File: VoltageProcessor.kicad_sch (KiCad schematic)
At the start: 29 parts, among them J1 PJ301M-12, J2 PJ301M-12, J3 Eurorack power, J4 PJ301M-12, J5 PJ301M-12, U1 TL074

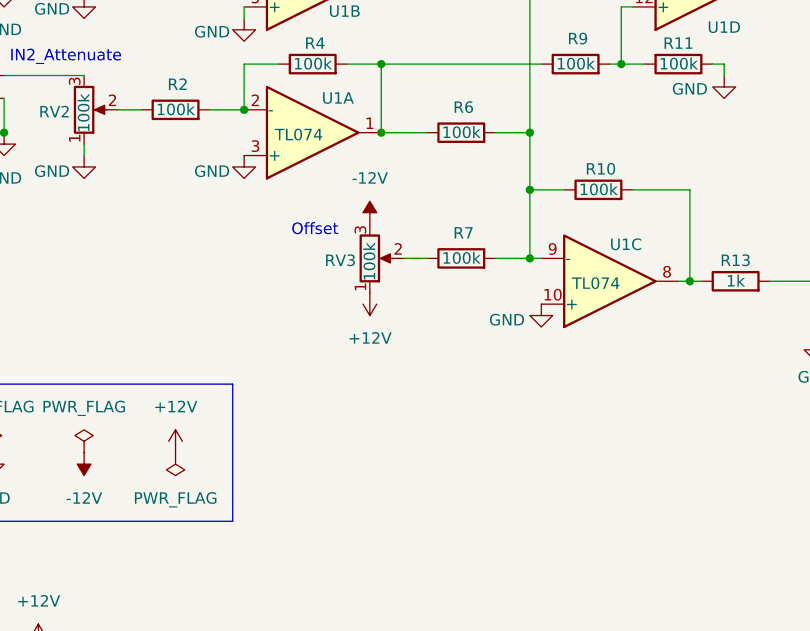
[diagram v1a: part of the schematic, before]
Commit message: Add `R15` `R16` to DC Offset potmeter its range is now `+-10` instead of the `rail-rail` voltage. Add small changes in routing to accomodate the resistors. Add change text to `rev 0.3`
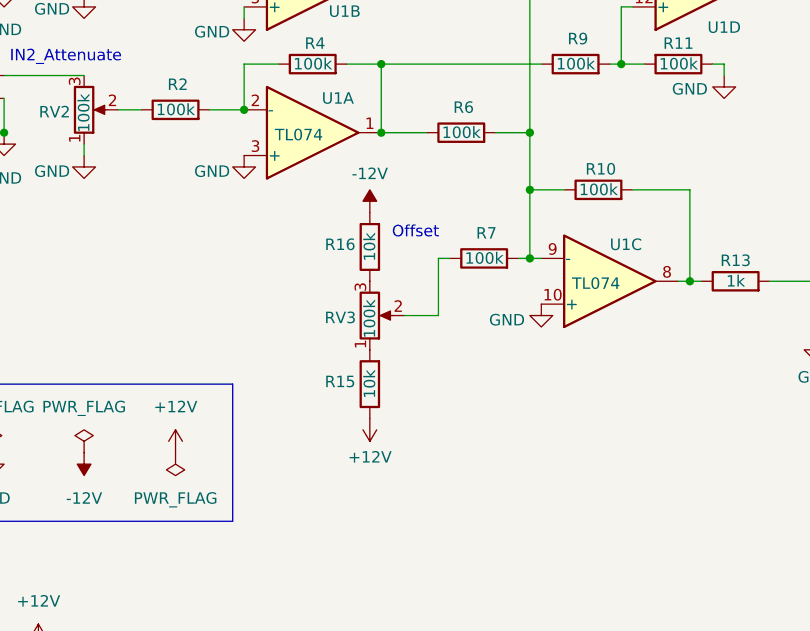
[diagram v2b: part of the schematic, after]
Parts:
- added R15, R16: 10k, Resistor_THT:R_Axial_DIN0204_L3.6mm_D1.6mm_P7.62mm_Horizontal, symbol Device:R
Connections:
- net +12V: now also R15.1; no longer RV3.1
- net -12V: now also R16.2; no longer RV3.3
- new net: R15.2, RV3.1
- new net: R16.1, RV3.3
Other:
- moved on the sheet: R7, RV3
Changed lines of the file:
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@@
 	)
 	(junction
-		(at 26.67 128.27)
+		(at 128.27 68.58)
 		(diameter 0)
 		(color 0 0 0 0)
 	)
 	(junction
-		(at 128.27 68.58)
+		(at 26.67 128.27)
 		(diameter 0)
 		(color 0 0 0 0)
@@
 	(wire
 		(pts
+			(xy 118.11 68.58) (xy 119.38 68.58)
+		)
+		(stroke
+			(width 0)
+			(type default)
+		)
+	)
+	(wire
+		(pts
 			(xy 82.55 35.56) (xy 85.09 35.56)
 		)
@@
 	(wire
 		(pts
+			(xy 114.3 74.93) (xy 118.11 74.93)
+		)
+		(stroke
+			(width 0)
+			(type default)
+		)
+	)
+	(wire
+		(pts
 			(xy 107.95 30.48) (xy 111.76 30.48)
 		)
@@
 	(wire
 		(pts
+			(xy 118.11 68.58) (xy 118.11 74.93)
+		)
+		(stroke
+			(width 0)
+			(type default)
+		)
+	)
+	(wire
+		(pts
 			(xy 129.54 68.58) (xy 128.27 68.58)
 		)
@@
 		)
 	)
-	(wire
-		(pts
-			(xy 114.3 68.58) (xy 116.84 68.58)
-		)
-		(stroke
-			(width 0)
-			(type default)
-		)
-	)
 	(polyline
 		(pts
@@
 	(wire
 		(pts
-			(xy 156.21 38.1) (xy 157.48 38.1)
+			(xy 127 68.58) (xy 128.27 68.58)
 		)
 		(stroke
@@
 	(wire
 		(pts
-			(xy 92.71 52.07) (xy 96.52 52.07)
+			(xy 156.21 38.1) (xy 157.48 38.1)
 		)
 		(stroke
@@
 	(wire
 		(pts
-			(xy 124.46 68.58) (xy 128.27 68.58)
+			(xy 92.71 52.07) (xy 96.52 52.07)
 		)
 		(stroke
@@
 	(text "Offset"
 		(exclude_from_sim no)
-		(at 104.394 65.532 0)
+		(at 115.57 65.786 0)
 		(effects
 			(font
@@
 	(symbol
 		(lib_id "power:+12V")
-		(at 110.49 72.39 180)
+		(at 110.49 86.36 180)
 		(unit 1)
 		(exclude_from_sim no)
@@
 		(on_board yes)
 		(dnp no)
-		(fields_autoplaced yes)
 		(property "Reference" "#PWR016"
-			(at 110.49 68.58 0)
+			(at 110.49 82.55 0)
 			(effects
 				(font
@@
 		)
 		(property "Value" "+12V"
-			(at 110.49 77.47 0)
+			(at 110.49 90.678 0)
 			(effects
 				(font
@@
 		)
 		(property "Footprint" ""
-			(at 110.49 72.39 0)
+			(at 110.49 86.36 0)
 			(effects
 				(font
@@
 		)
 		(property "Datasheet" ""
-			(at 110.49 72.39 0)
+			(at 110.49 86.36 0)
 			(effects
 				(font
@@
 		)
 		(property "Description" "Power symbol creates a global label with name \"+12V\""
-			(at 110.49 72.39 0)
+			(at 110.49 86.36 0)
 			(effects
 				(font
@@
 	(symbol
 		(lib_id "Device:R")
-		(at 120.65 68.58 90)
+		(at 123.19 68.58 90)
 		(unit 1)
 		(exclude_from_sim no)
@@
 		(dnp no)
 		(property "Reference" "R7"
-			(at 120.904 65.786 90)
+			(at 123.444 65.786 90)
 			(effects
 				(font
@@
 		)
 		(property "Value" "100k"
-			(at 120.65 68.58 90)
+			(at 123.19 68.58 90)
 			(effects
 				(font
@@
 		)
 		(property "Footprint" "Resistor_THT:R_Axial_DIN0204_L3.6mm_D1.6mm_P7.62mm_Horizontal"
-			(at 120.65 70.358 90)
+			(at 123.19 70.358 90)
 			(effects
 				(font
@@
 		)
 		(property "Datasheet" "~"
-			(at 120.65 68.58 0)
+			(at 123.19 68.58 0)
 			(effects
 				(font
@@
 		)
 		(property "Description" "Resistor"
-			(at 120.65 68.58 0)
+			(at 123.19 68.58 0)
 			(effects
 				(font
@@
 	(symbol
 		(lib_id "power:-12V")
-		(at 110.49 64.77 0)
+		(at 110.49 63.5 0)
 		(unit 1)
 		(exclude_from_sim no)
@@
 		(on_board yes)
 		(dnp no)
-		(fields_autoplaced yes)
 		(property "Reference" "#PWR015"
-			(at 110.49 68.58 0)
+			(at 110.49 67.31 0)
 			(effects
 				(font
@@
 		)
 		(property "Value" "-12V"
-			(at 110.49 59.69 0)
+			(at 110.49 59.182 0)
 			(effects
 				(font
@@
 		)
 		(property "Footprint" ""
-			(at 110.49 64.77 0)
+			(at 110.49 63.5 0)
 			(effects
 				(font
@@
 		)
 		(property "Datasheet" ""
-			(at 110.49 64.77 0)
+			(at 110.49 63.5 0)
 			(effects
 				(font
@@
 		)
 		(property "Description" "Power symbol creates a global label with name \"-12V\""
-			(at 110.49 64.77 0)
+			(at 110.49 63.5 0)
 			(effects
 				(font
@@
 	)
 	(symbol
+		(lib_id "Device:R")
+		(at 110.49 82.55 180)
+		(unit 1)
+		(exclude_from_sim no)
+		(in_bom yes)
+		(on_board yes)
+		(dnp no)
+		(property "Reference" "R15"
+			(at 107.188 82.296 0)
+			(effects
+				(font
+					(size 1.27 1.27)
+				)
+			)
+		)
+		(property "Value" "10k"
+			(at 110.49 82.55 90)
+			(effects
+				(font
+					(size 1.27 1.27)
+				)
+			)
+		)
+		(property "Footprint" "Resistor_THT:R_Axial_DIN0204_L3.6mm_D1.6mm_P7.62mm_Horizontal"
+			(at 112.268 82.55 90)
+			(effects
+				(font
+					(size 1.27 1.27)
+				)
+				(hide yes)
+			)
+		)
+		(property "Datasheet" "~"
+			(at 110.49 82.55 0)
+			(effects
+				(font
+					(size 1.27 1.27)
+				)
+				(hide yes)
+			)
+		)
+		(property "Description" "Resistor"
+			(at 110.49 82.55 0)
+			(effects
+				(font
+					(size 1.27 1.27)
+				)
+				(hide yes)
+			)
+		)
+		(pin "2"
+		)
+		(pin "1"
+		)
+		(instances
+			(project "VoltageProcessor"
+				(path "/4bee6c8d-ae50-4a17-b8d6-5e6212a77216"
+					(reference "R15")
+					(unit 1)
+				)
+			)
+		)
+	)
+	(symbol
 		(lib_id "Amplifier_Operational:TL074")
 		(at 104.14 54.61 0)
@@
 	)
 	(symbol
+		(lib_id "Device:R")
+		(at 110.49 67.31 180)
+		(unit 1)
+		(exclude_from_sim no)
+		(in_bom yes)
+		(on_board yes)
+		(dnp no)
+		(property "Reference" "R16"
+			(at 107.188 67.056 0)
+			(effects
+				(font
+					(size 1.27 1.27)
+				)
+			)
+		)
+		(property "Value" "10k"
+			(at 110.49 67.31 90)
+			(effects
+				(font
+					(size 1.27 1.27)
+				)
+			)
+		)
+		(property "Footprint" "Resistor_THT:R_Axial_DIN0204_L3.6mm_D1.6mm_P7.62mm_Horizontal"
+			(at 112.268 67.31 90)
+			(effects
+				(font
+					(size 1.27 1.27)
+				)
+				(hide yes)
+			)
+		)
+		(property "Datasheet" "~"
+			(at 110.49 67.31 0)
+			(effects
+				(font
+					(size 1.27 1.27)
+				)
+				(hide yes)
+			)
+		)
+		(property "Description" "Resistor"
+			(at 110.49 67.31 0)
+			(effects
+				(font
+					(size 1.27 1.27)
+				)
+				(hide yes)
+			)
+		)
+		(pin "2"
+		)
+		(pin "1"
+		)
+		(instances
+			(project "VoltageProcessor"
+				(path "/4bee6c8d-ae50-4a17-b8d6-5e6212a77216"
+					(reference "R16")
+					(unit 1)
+				)
+			)
+		)
+	)
+	(symbol
 		(lib_id "Device:R_Potentiometer")
-		(at 110.49 68.58 0)
+		(at 110.49 74.93 0)
 		(mirror x)
 		(unit 1)
@@
 		(dnp no)
 		(property "Reference" "RV3"
-			(at 108.966 68.834 0)
+			(at 108.966 75.184 0)
 			(effects
 				(font
@@
 		)
 		(property "Value" "100k"
-			(at 110.49 71.12 90)
+			(at 110.49 77.47 90)
 			(effects
 				(font
@@
 		)
 		(property "Footprint" "libararies:trimmer_alps-rk09k1130ah1"
-			(at 110.49 68.58 0)
+			(at 110.49 74.93 0)
 			(effects
 				(font
@@
 		)
 		(property "Datasheet" "~"
-			(at 110.49 68.58 0)
+			(at 110.49 74.93 0)
 			(effects
 				(font
@@
 		)
 		(property "Description" "Potentiometer"
-			(at 110.49 68.58 0)
+			(at 110.49 74.93 0)
 			(effects
 				(font
